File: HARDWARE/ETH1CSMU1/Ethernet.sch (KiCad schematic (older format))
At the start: 41 parts, among them U1001 LAN8742A, U1002 USBLC6-4, U1003 LC03-3.3, U1004 LC03-3.3, X1001 7M-25.000MAAJ-T

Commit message: Commit
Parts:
- C1005, C1006, C1007, C1008: footprint (none) -> SMD:C_0603_Symbol1
- L1001: value Ferrite_Bead -> MPZ2012S221A; footprint (none) -> SMD:R_0805_Symbol1
- R1003, R1007: footprint (none) -> SMD:R_0603_Symbol1
- R1005, R1008, R1009: value 10K -> 10k; footprint (none) -> SMD:R_0603_Symbol1
- R1020: footprint (none) -> SMD:R_0603_Symbol2
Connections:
- net GNDD: no longer C1001.2, C1002.2, C1003.2, C1004.2, C1005.2, C1006.2, C1007.2, C1008.2, C1009.2, C1010.1, C1011.2, R1003.2, R1014.2, R1016.2, R1017.2, U1001.25 (GND_EP), U1002.2 (GND), X1001.2 (GND), X1001.4 (GND)
- new net GND: C1001.2, C1002.2, C1003.2, C1004.2, C1005.2, C1006.2, C1007.2, C1008.2, C1009.2, C1010.1, C1011.2, R1003.2, R1014.2, R1016.2, R1017.2, U1001.25 (GND_EP), U1002.2 (GND), X1001.2 (GND), X1001.4 (GND)
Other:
- moved on the sheet: R1001, R1002, R1003, R1004, R1005, R1009, R1010, R1012, R1015, R1019

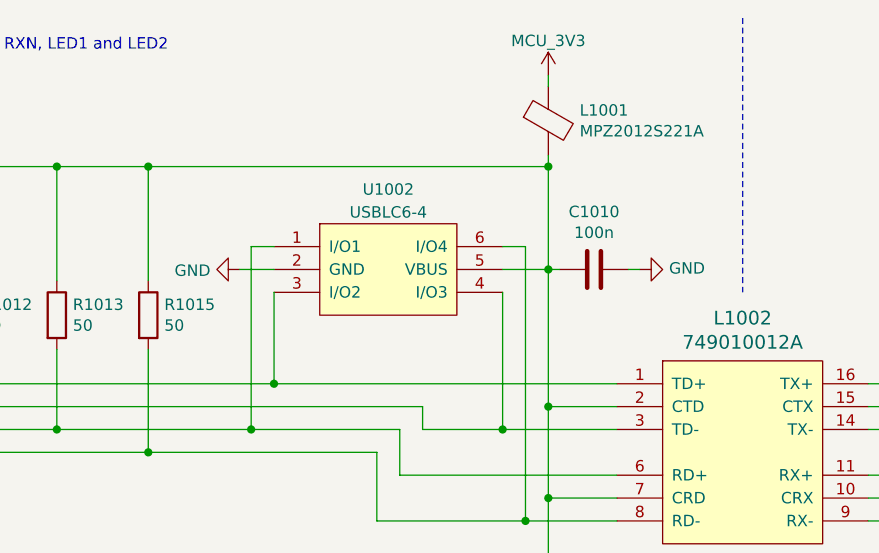
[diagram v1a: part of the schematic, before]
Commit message: Power schematic
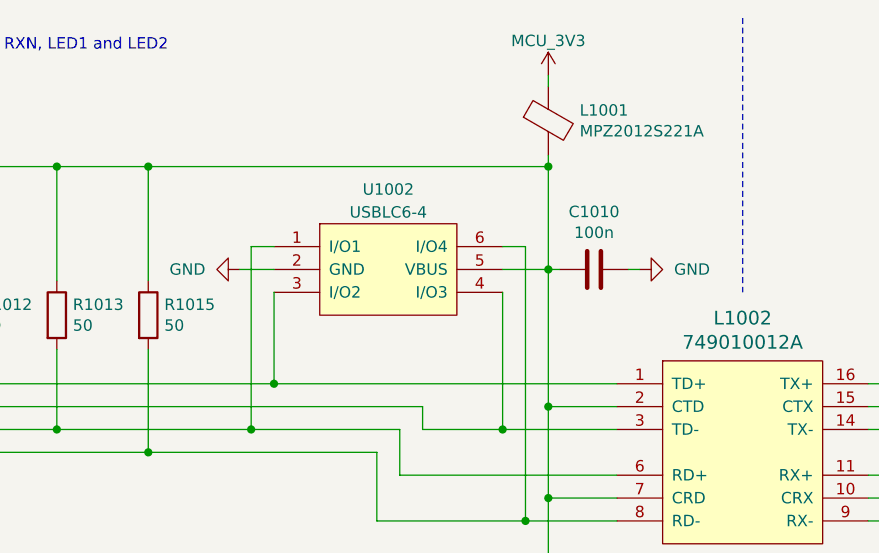
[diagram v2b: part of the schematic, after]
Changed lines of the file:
@@
 $Descr A4 11693 8268
 encoding utf-8
-Sheet 10 12
+Sheet 10 13
 Title ""
 Date ""
@@
 P 8450 1650
 F 0 "#PWR0104" H 8450 1400 50  0001 C CNN
-F 1 "GND" V 8455 1522 50  0000 R CNN
+F 1 "GND" V 8450 1500 50  0000 R CNN
 F 2 "" H 8450 1650 50  0001 C CNN
 F 3 "" H 8450 1650 50  0001 C CNN
@@
 P 6700 1650
 F 0 "#PWR0105" H 6700 1400 50  0001 C CNN
-F 1 "GND" V 6705 1522 50  0000 R CNN
+F 1 "GND" V 6700 1500 50  0000 R CNN
 F 2 "" H 6700 1650 50  0001 C CNN
 F 3 "" H 6700 1650 50  0001 C CNN

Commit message: Footprints
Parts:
- C1001, C1002, C1003: footprint (none) -> Capacitors_SMD:C_0603
- C1010: footprint (none) -> SMD:C_0603_Symbol1
- C1011, C1012: value 1n/2kV -> 1000p/2kV; footprint (none) -> Capacitors_SMD:C_1206
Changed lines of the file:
@@
 F 0 "C1003" H 5465 3696 50  0000 L CNN
 F 1 "470P" H 5465 3605 50  0000 L CNN
-F 2 "" H 5388 3500 50  0001 C CNN
+F 2 "Capacitors_SMD:C_0603" H 5388 3500 50  0001 C CNN
 F 3 "~" H 5350 3650 50  0001 C CNN
 	1    5350 3650
@@
 P 9700 3600
 F 0 "C1012" H 9815 3646 50  0000 L CNN
-F 1 "1n/2kV" H 9815 3555 50  0000 L CNN
-F 2 "" H 9738 3450 50  0001 C CNN
+F 1 "1000p/2kV" H 9815 3555 50  0000 L CNN
+F 2 "Capacitors_SMD:C_1206" H 9738 3450 50  0001 C CNN
 F 3 "~" H 9700 3600 50  0001 C CNN
 	1    9700 3600
@@
 P 8900 5300
 F 0 "C1011" V 8650 5300 50  0000 C CNN
-F 1 "1n/2kV" V 8750 5300 50  0000 C CNN
-F 2 "" H 8938 5150 50  0001 C CNN
+F 1 "1000p/2kV" V 8750 5300 50  0000 C CNN
+F 2 "Capacitors_SMD:C_1206" H 8938 5150 50  0001 C CNN
 F 3 "~" H 8900 5300 50  0001 C CNN
 	1    8900 5300
@@
 F 0 "C1010" V 7998 1650 50  0000 C CNN
 F 1 "100n" V 8089 1650 50  0000 C CNN
-F 2 "" H 8288 1500 50  0001 C CNN
+F 2 "SMD:C_0603_Symbol1" H 8288 1500 50  0001 C CNN
 F 3 "~" H 8250 1650 50  0001 C CNN
 	1    8250 1650
@@
 F 0 "C1001" H 1765 4846 50  0000 L CNN
 F 1 "30p" H 1765 4755 50  0000 L CNN
-F 2 "" H 1688 4650 50  0001 C CNN
+F 2 "Capacitors_SMD:C_0603" H 1688 4650 50  0001 C CNN
 F 3 "~" H 1650 4800 50  0001 C CNN
 	1    1650 4800
@@
 F 0 "C1002" H 2865 4846 50  0000 L CNN
 F 1 "30p" H 2865 4755 50  0000 L CNN
-F 2 "" H 2788 4650 50  0001 C CNN
+F 2 "Capacitors_SMD:C_0603" H 2788 4650 50  0001 C CNN
 F 3 "~" H 2750 4800 50  0001 C CNN
 	1    2750 4800

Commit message: Footprint selection
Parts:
- C1003: value 470P -> 470p
- C1004: value 1U -> 1u
- D1001, D1002: footprint (none) -> LEDs:LED_0603
- R1001, R1002, R1004, R1006, R1011, R1014, R1016, R1018, R1019: footprint (none) -> Resistors_SMD:R_0603
- R1010, R1012, R1013, R1015: footprint (none) -> SMD:R_0603_Symbol4
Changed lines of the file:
@@
 F 0 "R1001" V 1750 2300 50  0000 C CNN
 F 1 "33" V 1800 2550 50  0000 C CNN
-F 2 "" V 1730 2550 50  0001 C CNN
+F 2 "Resistors_SMD:R_0603" V 1730 2550 50  0001 C CNN
 F 3 "~" H 1800 2550 50  0001 C CNN
 	1    1800 2550
@@
 F 0 "R1002" V 1750 2400 50  0000 C CNN
 F 1 "33" V 1800 2650 50  0000 C CNN
-F 2 "" V 1730 2650 50  0001 C CNN
+F 2 "Resistors_SMD:R_0603" V 1730 2650 50  0001 C CNN
 F 3 "~" H 1800 2650 50  0001 C CNN
 	1    1800 2650
@@
 F 0 "R1006" V 2450 3100 50  0000 C CNN
 F 1 "1k5" V 2550 3100 50  0000 C CNN
-F 2 "" V 2480 3100 50  0001 C CNN
+F 2 "Resistors_SMD:R_0603" V 2480 3100 50  0001 C CNN
 F 3 "~" H 2550 3100 50  0001 C CNN
 	1    2550 3100
@@
 F 0 "R1010" H 5170 1896 50  0000 L CNN
 F 1 "50" H 5170 1805 50  0000 L CNN
-F 2 "" V 5030 1850 50  0001 C CNN
+F 2 "SMD:R_0603_Symbol4" V 5030 1850 50  0001 C CNN
 F 3 "~" H 5100 1850 50  0001 C CNN
 	1    5100 1850
@@
 F 0 "R1012" H 5570 1896 50  0000 L CNN
 F 1 "50" H 5570 1805 50  0000 L CNN
-F 2 "" V 5430 1850 50  0001 C CNN
+F 2 "SMD:R_0603_Symbol4" V 5430 1850 50  0001 C CNN
 F 3 "~" H 5500 1850 50  0001 C CNN
 	1    5500 1850
@@
 F 0 "R1013" H 5970 1896 50  0000 L CNN
 F 1 "50" H 5970 1805 50  0000 L CNN
-F 2 "" V 5830 1850 50  0001 C CNN
+F 2 "SMD:R_0603_Symbol4" V 5830 1850 50  0001 C CNN
 F 3 "~" H 5900 1850 50  0001 C CNN
 	1    5900 1850
@@
 F 0 "R1015" H 6370 1896 50  0000 L CNN
 F 1 "50" H 6370 1805 50  0000 L CNN
-F 2 "" V 6230 1850 50  0001 C CNN
+F 2 "SMD:R_0603_Symbol4" V 6230 1850 50  0001 C CNN
 F 3 "~" H 6300 1850 50  0001 C CNN
 	1    6300 1850
@@
 P 5350 3650
 F 0 "C1003" H 5465 3696 50  0000 L CNN
-F 1 "470P" H 5465 3605 50  0000 L CNN
+F 1 "470p" H 5465 3605 50  0000 L CNN
 F 2 "Capacitors_SMD:C_0603" H 5388 3500 50  0001 C CNN
 F 3 "~" H 5350 3650 50  0001 C CNN
@@
 P 5800 3650
 F 0 "C1004" H 5915 3696 50  0000 L CNN
-F 1 "1U" H 5915 3605 50  0000 L CNN
+F 1 "1u" H 5915 3605 50  0000 L CNN
 F 2 "" H 5838 3500 50  0001 C CNN
 F 3 "~" H 5800 3650 50  0001 C CNN
@@
 F 0 "R1011" V 5150 2950 50  0000 C CNN
 F 1 "12K1" V 5250 2950 50  0000 C CNN
-F 2 "" V 5180 2950 50  0001 C CNN
+F 2 "Resistors_SMD:R_0603" V 5180 2950 50  0001 C CNN
 F 3 "~" H 5250 2950 50  0001 C CNN
 	1    5250 2950
@@
 F 0 "R1018" H 9570 3246 50  0000 L CNN
 F 1 "75" H 9570 3155 50  0000 L CNN
-F 2 "" V 9430 3200 50  0001 C CNN
+F 2 "Resistors_SMD:R_0603" V 9430 3200 50  0001 C CNN
 F 3 "~" H 9500 3200 50  0001 C CNN
 	1    9500 3200
@@
 F 0 "R1019" H 9970 3246 50  0000 L CNN
 F 1 "75" H 9970 3155 50  0000 L CNN
-F 2 "" V 9830 3200 50  0001 C CNN
+F 2 "Resistors_SMD:R_0603" V 9830 3200 50  0001 C CNN
 F 3 "~" H 9900 3200 50  0001 C CNN
 	1    9900 3200
@@
 F 0 "D1001" V 6038 4882 50  0000 R CNN
 F 1 "GREEN" V 5947 4882 50  0000 R CNN
-F 2 "" H 6000 5000 50  0001 C CNN
+F 2 "LEDs:LED_0603" H 6000 5000 50  0001 C CNN
 F 3 "~" H 6000 5000 50  0001 C CNN
 	1    6000 5000
@@
 F 0 "D1002" V 6538 4882 50  0000 R CNN
 F 1 "YELLOW" V 6447 4882 50  0000 R CNN
-F 2 "" H 6500 5000 50  0001 C CNN
+F 2 "LEDs:LED_0603" H 6500 5000 50  0001 C CNN
 F 3 "~" H 6500 5000 50  0001 C CNN
 	1    6500 5000
@@
 F 0 "R1014" H 6070 5446 50  0000 L CNN
 F 1 "270" H 6070 5355 50  0000 L CNN
-F 2 "" V 5930 5400 50  0001 C CNN
+F 2 "Resistors_SMD:R_0603" V 5930 5400 50  0001 C CNN
 F 3 "~" H 6000 5400 50  0001 C CNN
 	1    6000 5400
@@
 F 0 "R1016" H 6570 5446 50  0000 L CNN
 F 1 "270" H 6570 5355 50  0000 L CNN
-F 2 "" V 6430 5400 50  0001 C CNN
+F 2 "Resistors_SMD:R_0603" V 6430 5400 50  0001 C CNN
 F 3 "~" H 6500 5400 50  0001 C CNN
 	1    6500 5400
@@
 F 0 "R1004" V 1750 2700 50  0000 C CNN
 F 1 "33" V 1800 2950 50  0000 C CNN
-F 2 "" V 1730 2950 50  0001 C CNN
+F 2 "Resistors_SMD:R_0603" V 1730 2950 50  0001 C CNN
 F 3 "~" H 1800 2950 50  0001 C CNN
 	1    1800 2950

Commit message: Redesigned feedback circuit.
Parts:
- L1002: footprint (none) -> SMD:Wurth_749010012A
- U1001: footprint (none) -> Housings_DFN_QFN:QFN-24-1EP_4x4mm_Pitch0.5mm
- U1002: footprint (none) -> TO_SOT_Packages_SMD:SOT-23-6
- U1003, U1004: footprint (none) -> SMD:SO8E
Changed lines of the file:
@@
 F 0 "U1001" H 3950 4115 50  0000 C CNN
 F 1 "LAN8742A" H 3950 4024 50  0000 C CNN
-F 2 "" H 4100 4050 50  0001 C CNN
+F 2 "Housings_DFN_QFN:QFN-24-1EP_4x4mm_Pitch0.5mm" H 4100 4050 50  0001 C CNN
 F 3 "" H 4100 4050 50  0001 C CNN
 	1    3950 3000
@@
 F 0 "L1002" H 8900 3037 60  0000 C CNN
 F 1 "749010012A" H 8900 2931 60  0000 C CNN
-F 2 "" H 10800 2550 60  0001 C CNN
+F 2 "SMD:Wurth_749010012A" H 10800 2550 60  0001 C CNN
 F 3 "" H 10800 2550 60  0000 C CNN
 	1    8900 2450
@@
 F 0 "U1003" H 10500 2487 60  0000 C CNN
 F 1 "LC03-3.3" H 10500 2381 60  0000 C CNN
-F 2 "" H 10500 2050 60  0001 C CNN
+F 2 "SMD:SO8E" H 10500 2050 60  0001 C CNN
 F 3 "" H 10500 2050 60  0000 C CNN
 	1    10500 2050
@@
 F 0 "U1004" H 10500 3287 60  0000 C CNN
 F 1 "LC03-3.3" H 10500 3181 60  0000 C CNN
-F 2 "" H 10500 2850 60  0001 C CNN
+F 2 "SMD:SO8E" H 10500 2850 60  0001 C CNN
 F 3 "" H 10500 2850 60  0000 C CNN
 	1    10500 2850
@@
 F 0 "U1002" H 7350 2000 50  0000 C CNN
 F 1 "USBLC6-4" H 7350 1900 50  0000 C CNN
-F 2 "" H 7250 1850 50  0001 C CNN
+F 2 "TO_SOT_Packages_SMD:SOT-23-6" H 7250 1850 50  0001 C CNN
 F 3 "" H 7250 1850 50  0001 C CNN
 	1    7350 1650

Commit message: Added MUX schematic
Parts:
- R1017: footprint (none) -> Resistors_SMD:R_1206
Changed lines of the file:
@@
 $Descr A4 11693 8268
 encoding utf-8
-Sheet 10 13
+Sheet 10 14
 Title ""
 Date ""
@@
 F 0 "R1017" V 8700 4900 50  0000 C CNN
 F 1 "1Meg/1kV" V 8800 4900 50  0000 C CNN
-F 2 "" V 8830 4900 50  0001 C CNN
+F 2 "Resistors_SMD:R_1206" V 8830 4900 50  0001 C CNN
 F 3 "~" H 8900 4900 50  0001 C CNN
 	1    8900 4900

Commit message: Schematic development
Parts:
- renumbered C1001 to C901, C1002 to C902, C1003 to C903, C1004 to C904, C1005 to C905, C1006 to C906, C1007 to C907, C1008 to C908, C1009 to C909, C1010 to C910, C1011 to C911, C1012 to C912, D1001 to D901, D1002 to D902, L1001 to L901, L1002 to L902, R1020 to R901, R1001 to R902, R1002 to R903, R1003 to R904, R1004 to R905, R1005 to R906, R1008 to R907, R1006 to R908, R1007 to R909, R1009 to R910, R1010 to R911, R1011 to R912, R1012 to R913, R1013 to R914, R1014 to R915, R1015 to R916, R1016 to R917, R1017 to R918, R1018 to R919, R1019 to R920, U1001 to U901, U1002 to U902, U1003 to U903, U1004 to U904, X1001 to X901

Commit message: check in
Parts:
- X901: footprint (none) -> SMD:7M
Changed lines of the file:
@@
 F 0 "X901" H 2050 5250 60  0000 L CNN
 F 1 "7M-25.000MAAJ-T" H 1800 5150 60  0000 L CNN
-F 2 "" H 2200 4600 60  0001 C CNN
+F 2 "SMD:7M" H 2200 4600 60  0001 C CNN
 F 3 "" H 2200 4600 60  0000 C CNN
 	1    2200 4600
